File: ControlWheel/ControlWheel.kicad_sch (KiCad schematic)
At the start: 1 part, among them U1 AI12

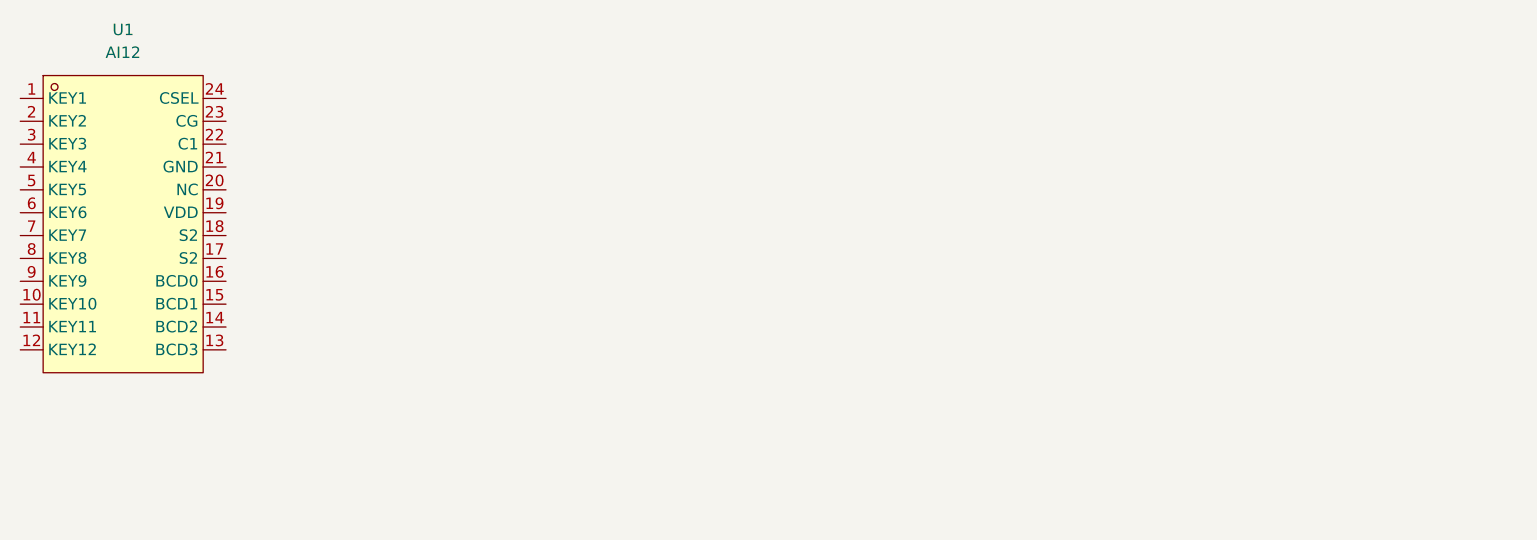
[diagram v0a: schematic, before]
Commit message: footprints for wheel + power changes for v3s
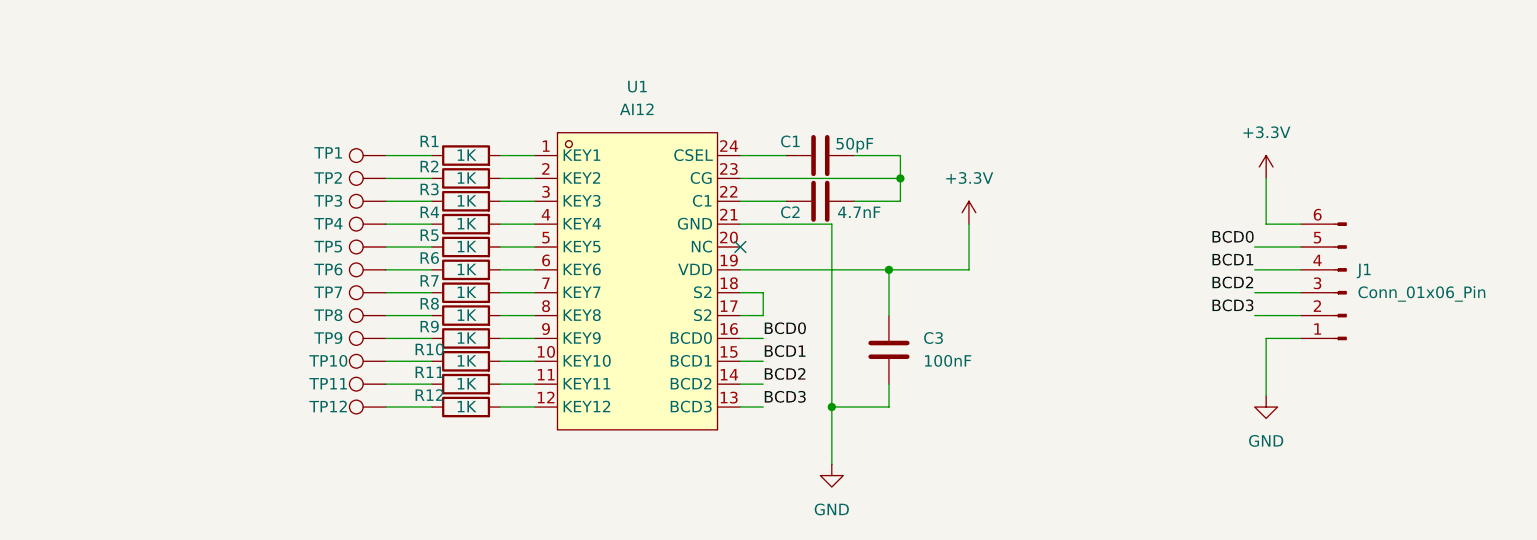
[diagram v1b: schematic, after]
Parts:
- added C1: 50pF, symbol Device:C
- added C2: 4.7nF, symbol Device:C
- added C3: 100nF, symbol Device:C
- added J1: Conn_01x06_Pin, FlexPCB_FPC:6pin_0.5mm-Pitch, symbol Connector:Conn_01x06_Pin
- added R1, R10, R11, R12, R2, R3, R4, R5, R6, R7, R8, R9: 1K, symbol Device:R
- added TP1, TP10, TP11, TP12, TP2, TP3, TP4, TP5, TP6, TP7, TP8, TP9: TestPoint, CapTouchPads:RoundPad, symbol Connector:TestPoint
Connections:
- net at U1.1 (KEY1): now also R1.2
- net at U1.10 (KEY10): now also R10.2
- net at U1.11 (KEY11): now also R11.2
- net at U1.12 (KEY12): now also R12.2
- net BCD3: now reaches U1.13 (BCD3)
- net BCD3: now also J1.2 (Pin_2)
- net BCD2: now reaches U1.14 (BCD2)
- net BCD2: now also J1.3 (Pin_3)
- net BCD1: now reaches U1.15 (BCD1)
- net BCD1: now also J1.4 (Pin_4)
- net BCD0: now reaches U1.16 (BCD0)
- net BCD0: now also J1.5 (Pin_5)
- net at U1.17 (S2): now also U1.18 (S2)
- net +3.3V: now reaches U1.19 (VDD)
- net +3.3V: now also C3.1, J1.6 (Pin_6)
- net at U1.2 (KEY2): now also R2.2
- net GND: now reaches U1.21 (GND)
- net GND: now also C3.2, J1.1 (Pin_1)
- net at U1.22 (C1): now also C2.1
- net at U1.23 (CG): now also C1.2, C2.2
- net at U1.24 (CSEL): now also C1.1
- net at U1.3 (KEY3): now also R3.2
- net at U1.4 (KEY4): now also R4.2
- net at U1.5 (KEY5): now also R5.2
- net at U1.6 (KEY6): now also R6.2
- net at U1.7 (KEY7): now also R7.2
- net at U1.8 (KEY8): now also R8.2
- net at U1.9 (KEY9): now also R9.2
- new net: R9.1, TP9.1
- new net: R11.1, TP11.1
- new net: R8.1, TP8.1
- new net: R3.1, TP3.1
- new net: R10.1, TP10.1
- new net: R2.1, TP2.1
- new net: R7.1, TP7.1
- new net: R5.1, TP5.1
- new net: R6.1, TP6.1
- new net: R12.1, TP12.1
- new net: R1.1, TP1.1
- new net: R4.1, TP4.1
- no-connect marks 0 -> 1
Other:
- moved on the sheet: U1
